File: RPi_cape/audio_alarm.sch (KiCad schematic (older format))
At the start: 83 parts, among them J13 Conn_01x02, J14 Conn_01x02, Q11 MMBT3904, Q12 MMBT3906, Q13 MMBT3904, Q2 MMBT3904, Q5 MMBT3904, Q6 MMBT3904, Q7 DNP, Q8 MMBT3904, U24 TL431A, U25 LM2903, U26 MIC1557, U27 MIC1557, U28 LM4871M

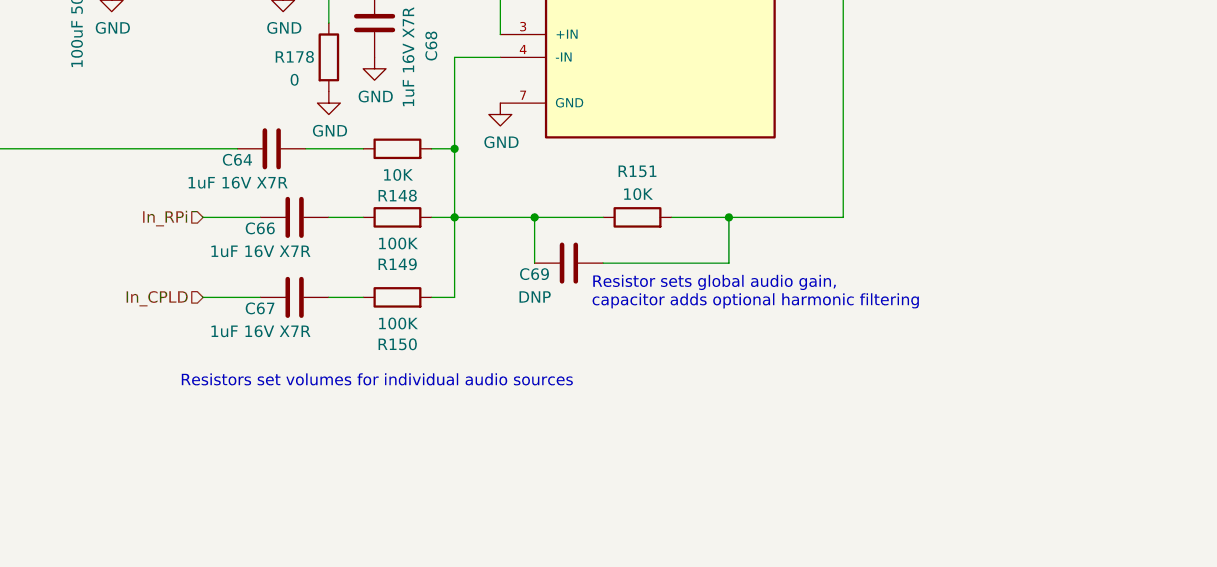
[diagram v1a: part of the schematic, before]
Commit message: Updates based on testing, extra documentation
Added thermal calculations, possible thermal-induced problems to fault-condition list
Renamed error calculations file
Added some bringup tests
Changed 24V LED resistors (R20, R22) to 24.9K to consolidate BOM
Adjusted audio amp volume and filtering according to breadboard experiments
Moved bottom-end mounting holes and encoder connectors to avoid interfering mechanically with Raspberry Pi
Replaced under-sized power-ORing diodes with better Schottky option, added heatsinking with copper planes
Improved LMZ14203 heatsinking by removing thermal reliefs, re-arranging input-current-measurement testpoints to increase top-layer copper area
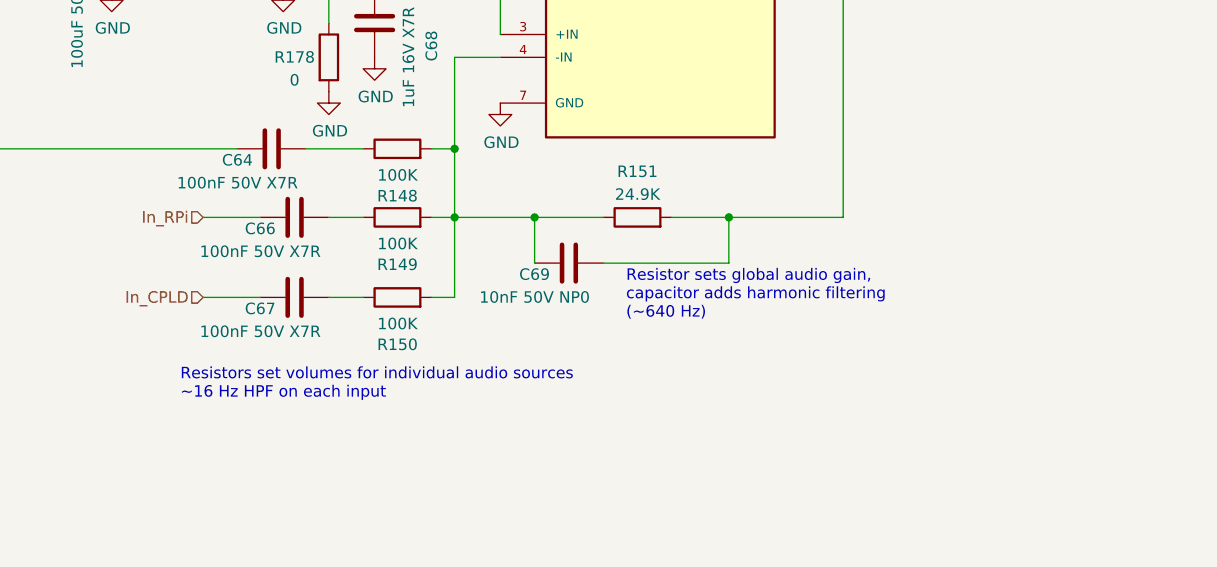
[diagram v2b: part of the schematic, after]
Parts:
- C64, C66, C67: value 1uF 16V X7R -> 100nF 50V X7R; footprint Capacitor_SMD:C_0805_2012Metric -> Capacitor_SMD:C_0603_1608Metric; Manufacturer Kemet -> AVX; Part Number C0805C105K4RACTU -> 06035C104JAT2A
- C69: value DNP -> 10nF 50V NP0; footprint Capacitor_SMD:C_0805_2012Metric -> Capacitor_SMD:C_0603_1608Metric; Manufacturer (none) -> Murata; Part Number (none) -> GRM1885C1H103JA01D
- R148: value 10K -> 100K; Part Number RK73H2BTTD1002F -> RK73H2BTTD1003F
- R151: value 10K -> 24.9K; Part Number RK73H2BTTD1002F -> RK73H2BTTD2492F
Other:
- note added: "Resistor sets global audio gain,\ncapacitor adds harmonic filtering\n(~~640 Hz)"
- note added: "Resistors set volumes for individual audio sources\n~~16 Hz HPF on each input"
- note removed: "Resistor sets global audio gain,\ncapacitor adds optional harmonic filtering"
- note removed: "Resistors set volumes for individual audio sources"
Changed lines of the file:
@@
 Title "Raspberry Pi Hat for JamVent Adaptation"
 Date ""
-Rev "1.8"
+Rev "1.9"
 Comp "US JamVent Team"
 Comment1 "Don Straney"
@@
 AR Path="/5E8E1F08/5F17DF13" Ref="R151"  Part="1"
 F 0 "R151" V 10400 2650 50  0000 C CNN
-F 1 "10K" V 10300 2650 50  0000 C CNN
+F 1 "24.9K" V 10300 2650 50  0000 C CNN
 F 2 "Resistor_SMD:R_1206_3216Metric" V 10130 2650 50  0001 C CNN
 F 3 "~" H 10200 2650 50  0001 C CNN
 F 4 "KOA Speer" H 10200 2650 50  0001 C CNN "Manufacturer"
-F 5 "RK73H2BTTD1002F" H 10200 2650 50  0001 C CNN "Part Number"
+F 5 "RK73H2BTTD2492F" H 10200 2650 50  0001 C CNN "Part Number"
 	1    10200 2650
 	0    -1   -1   0
@@
 AR Path="/5E8E1F08/5F18A428" Ref="R148"  Part="1"
 F 0 "R148" V 8943 2350 50  0000 C CNN
-F 1 "10K" V 9034 2350 50  0000 C CNN
+F 1 "100K" V 9034 2350 50  0000 C CNN
 F 2 "Resistor_SMD:R_1206_3216Metric" V 9080 2350 50  0001 C CNN
 F 3 "~" H 9150 2350 50  0001 C CNN
 F 4 "KOA Speer" H 9150 2350 50  0001 C CNN "Manufacturer"
-F 5 "RK73H2BTTD1002F" H 9150 2350 50  0001 C CNN "Part Number"
+F 5 "RK73H2BTTD1003F" H 9150 2350 50  0001 C CNN "Part Number"
 	1    9150 2350
 	0    -1   -1   0
@@
 AR Path="/5E8E1F08/5F192E05" Ref="C64"  Part="1"
 F 0 "C64" V 8550 2500 50  0000 C CNN
-F 1 "1uF 16V X7R" V 8450 2500 50  0000 C CNN
-F 2 "Capacitor_SMD:C_0805_2012Metric" H 8638 2200 50  0001 C CNN
+F 1 "100nF 50V X7R" V 8450 2500 50  0000 C CNN
+F 2 "Capacitor_SMD:C_0603_1608Metric" H 8638 2200 50  0001 C CNN
 F 3 "~" H 8600 2350 50  0001 C CNN
-F 4 "Kemet" H 8600 2350 50  0001 C CNN "Manufacturer"
-F 5 "C0805C105K4RACTU" H 8600 2350 50  0001 C CNN "Part Number"
+F 4 "AVX" H 8600 2350 50  0001 C CNN "Manufacturer"
+F 5 "06035C104JAT2A" H 8600 2350 50  0001 C CNN "Part Number"
 	1    8600 2350
 	0    -1   -1   0
@@
 AR Path="/5E8E1F08/5F1933A7" Ref="C66"  Part="1"
 F 0 "C66" V 8650 2800 50  0000 C CNN
-F 1 "1uF 16V X7R" V 8550 2800 50  0000 C CNN
-F 2 "Capacitor_SMD:C_0805_2012Metric" H 8738 2500 50  0001 C CNN
+F 1 "100nF 50V X7R" V 8550 2800 50  0000 C CNN
+F 2 "Capacitor_SMD:C_0603_1608Metric" H 8738 2500 50  0001 C CNN
 F 3 "~" H 8700 2650 50  0001 C CNN
-F 4 "Kemet" H 8700 2650 50  0001 C CNN "Manufacturer"
-F 5 "C0805C105K4RACTU" H 8700 2650 50  0001 C CNN "Part Number"
+F 4 "AVX" H 8700 2650 50  0001 C CNN "Manufacturer"
+F 5 "06035C104JAT2A" H 8700 2650 50  0001 C CNN "Part Number"
 	1    8700 2650
 	0    -1   -1   0
@@
 AR Path="/5E8E1F08/5F19381A" Ref="C67"  Part="1"
 F 0 "C67" V 8650 3150 50  0000 C CNN
-F 1 "1uF 16V X7R" V 8550 3150 50  0000 C CNN
-F 2 "Capacitor_SMD:C_0805_2012Metric" H 8738 2850 50  0001 C CNN
+F 1 "100nF 50V X7R" V 8550 3150 50  0000 C CNN
+F 2 "Capacitor_SMD:C_0603_1608Metric" H 8738 2850 50  0001 C CNN
 F 3 "~" H 8700 3000 50  0001 C CNN
-F 4 "Kemet" H 8700 3000 50  0001 C CNN "Manufacturer"
-F 5 "C0805C105K4RACTU" H 8700 3000 50  0001 C CNN "Part Number"
+F 4 "AVX" H 8700 3000 50  0001 C CNN "Manufacturer"
+F 5 "06035C104JAT2A" H 8700 3000 50  0001 C CNN "Part Number"
 	1    8700 3000
 	0    -1   -1   0
@@
 Wire Wire Line
 	8750 2350 9000 2350
-Text Notes 8200 3400 0    50   ~ 0
-Resistors set volumes for individual audio sources
-Text Notes 10000 3050 0    50   ~ 0
-Resistor sets global audio gain,\ncapacitor adds optional harmonic filtering
+Text Notes 8200 3450 0    50   ~ 0
+Resistors set volumes for individual audio sources\n~~16 Hz HPF on each input
+Text Notes 10150 3100 0    50   ~ 0
+Resistor sets global audio gain,\ncapacitor adds harmonic filtering\n(~~640 Hz)
 $Comp
 L Device:C C?
@@
 AR Path="/5E8E1F08/5F19C623" Ref="C69"  Part="1"
 F 0 "C69" V 9850 3000 50  0000 C CNN
-F 1 "DNP" V 9750 3000 50  0000 C CNN
-F 2 "Capacitor_SMD:C_0805_2012Metric" H 9938 2700 50  0001 C CNN
+F 1 "10nF 50V NP0" V 9750 3000 50  0000 C CNN
+F 2 "Capacitor_SMD:C_0603_1608Metric" H 9938 2700 50  0001 C CNN
 F 3 "~" H 9900 2850 50  0001 C CNN
+F 4 "Murata" H 9900 2850 50  0001 C CNN "Manufacturer"
+F 5 "GRM1885C1H103JA01D" H 9900 2850 50  0001 C CNN "Part Number"
 	1    9900 2850
 	0    -1   -1   0

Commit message: Design update based on changed software/firmware/pneumatics reqs
Swapped Max V CPLD for Max 10 FPGA
Removed +1.8V regulator and monitoring (in power-down alarm) because Max 10 FPGA has internal regulator
Changed FPGA's valve-enable pull-downs from 1K to 10K because Max 10 floats the outputs during power-up/programming (instead of Max V's internal pull-ups)
Changed low-pressure sensor from BMP388 to MS5607 for more manufacturable footprint / high availability, and moved all digital pressure sensors to daughterboard for repairability
Changed single op-amps in analog pressure sensor inputs / valve motion detect circuits to TLV6001 for better bias current, correct footprint
Removed excessive DNP components in analog pressure sensor inputs to ease routing with new op-amps
Added double-inverted hysteresis circuit to valve motion detect that won't drive U38's '+' input above the rail and cause latchup
Added optional pull-down resistors to valve-motiion-detect op-amps to allow output voltages to swing to zero
Added optional filter caps to ADC sensor inputs
Added pull-down to O2 sensor input for testing with sensor unplugged
Increased ADC input resistors (in analog sensor inputs) from 1K to 3.3K to avoid "lifting" +3.3V rail voltage in case of fault
Increased hole sizes to 3.7 mm for fitting #6 screws, to match some threaded vibration-damping bumpers from Joost
Fixed F.Fab-layer component reference text in custom footprints
Updated manufacturing files
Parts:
- removed D14, D40: BAS21AH, Ventilator:D_SOD-323, symbol Device:D_ALT
- removed Q6: MMBT3904, Ventilator:SOT-23, symbol Transistor_BJT:MMBT3904
- removed R130: 1K, Resistor_SMD:R_1206_3216Metric, symbol Device:R
- removed R131, R132: 10K, Resistor_SMD:R_1206_3216Metric, symbol Device:R
- added D33: BAS21AH, Ventilator:D_SOD-323, symbol Device:D_ALT
- added Q3: MMBT3904, Ventilator:SOT-23, symbol Transistor_BJT:MMBT3904
- added R37: 100K, Resistor_SMD:R_1206_3216Metric, symbol Device:R
- D28, D38, D39, J13, J14, Q7, R133, R134, R135, R145, R189: DNI (none) -> DNI
- J22: renamed from BT1; value 4x AA -> Conn_01x02; DNI (none) -> DNI
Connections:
- net +3V3: now also R37.2
- net GND: now also Q3.2 (E)
- net at D41.2 (A), Q5.3 (C), R129.1: now also D33.1 (K)
- new net: D33.2 (A), Q3.1 (B), R37.1
- new net ~FPGA_RST: Q3.3 (C)
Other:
- note added: "4x AA"
- note added: "Keeps FPGA from\nloading config.\nuntil +3.3V rail\nis high enough"
- note removed: "Threshold ~~0.9-1.4V"
- moved on the sheet: D38, D39, Q7, R133, R134, R135
